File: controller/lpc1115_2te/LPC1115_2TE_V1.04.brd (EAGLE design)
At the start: 30.5 x 58.1 mm, 59 parts, among them IC1 LPC1115, IC2 BD9G101, Q1 BC856, Q2 BC847C, Q3 BCP52, Q4 ASFL

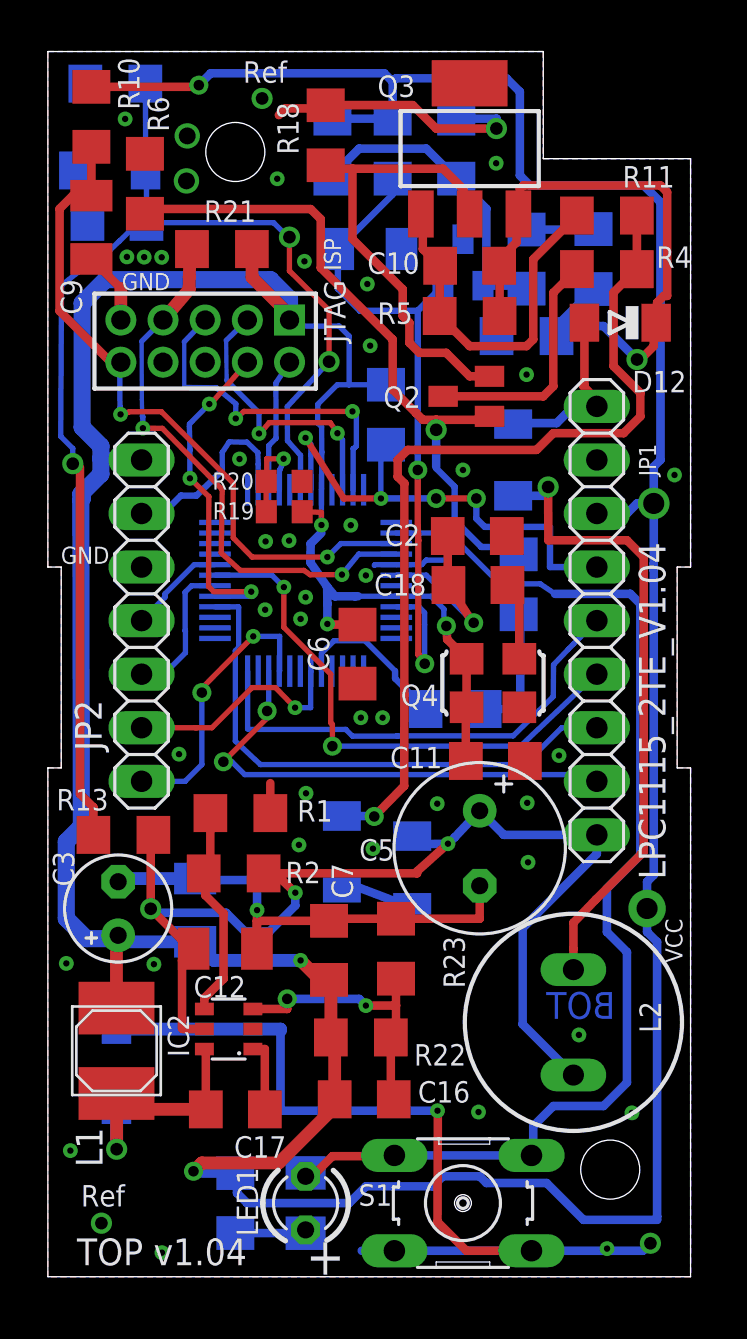
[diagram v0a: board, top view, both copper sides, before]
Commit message: Id-resistor package changed to 1206 and replace.
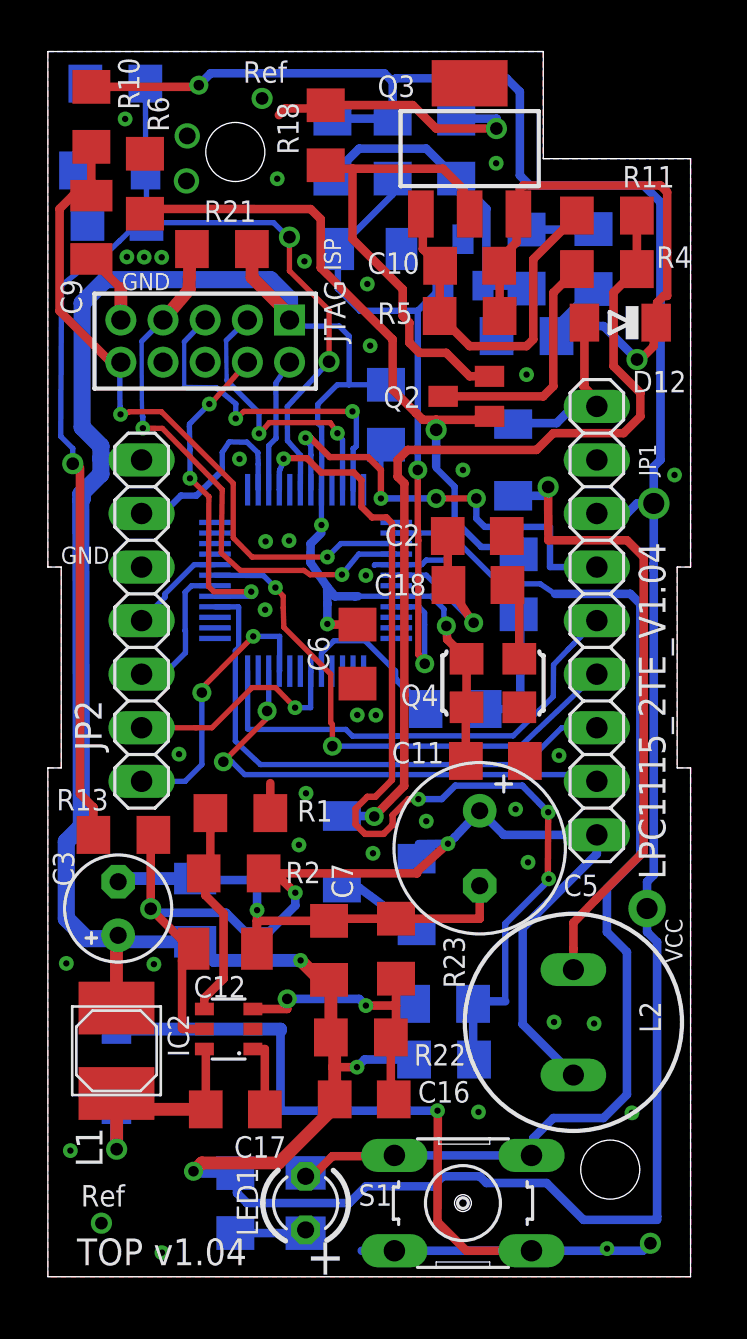
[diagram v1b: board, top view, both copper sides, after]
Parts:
- R19, R20: device rcl:R0603 -> rcl:R1206
- moved R19 27.1 mm to (18.8, 10.3), flipped to the bottom
- moved R20 25.9 mm to (18.7, 12.9), flipped to the bottom
- moved D3 1.09 mm to (17.5, 18.1)
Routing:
- net IO12: track 4.99 -> 49.1 mm, vias 1 -> 4
- net VCC: track 230.0 -> 232.4 mm, vias 8 -> 9
- net N$15: track 3.51 -> 4.21 mm
- net GND: track 91.3 -> 91.1 mm, vias 46 -> 44
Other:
- board text removed: "BOT"
